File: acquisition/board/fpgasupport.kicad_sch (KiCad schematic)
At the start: 62 parts, among them J1 XILINX_JTAG, U2 XC7A50T-1FTG256C, U6 ICE40UP5K_QFN48

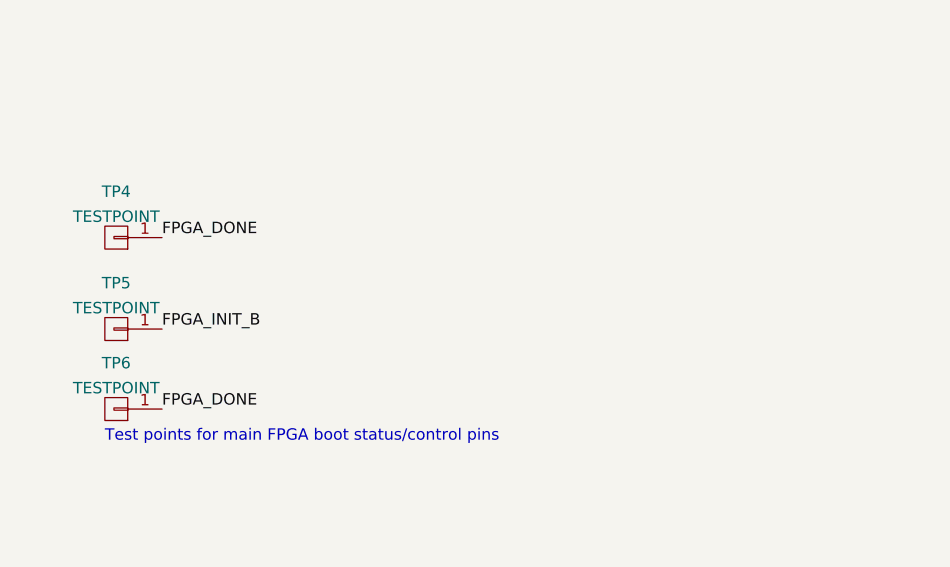
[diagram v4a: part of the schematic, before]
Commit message: Completed schematic after design review, ready for layout
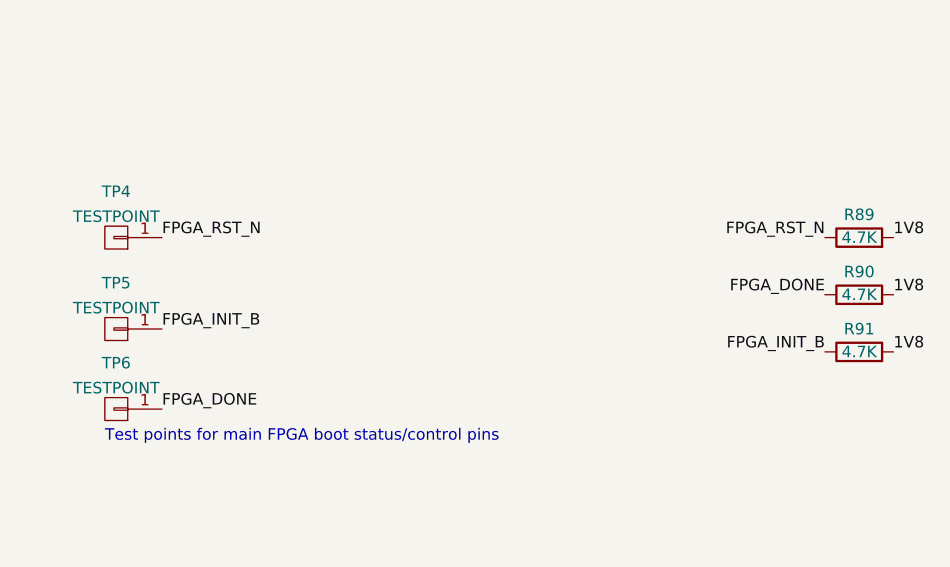
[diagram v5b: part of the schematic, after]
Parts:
- added R89, R90, R91: 4.7K, symbol device:R
- C41, C50: footprint (none) -> azonenberg_pcb:EIA_1210_CAP_NOSILK
- C42, C46: footprint (none) -> azonenberg_pcb:EIA_1206_CAP_NOSILK
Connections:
- net 1V8: now also R89.2, R90.2, R91.2
- net FPGA_DONE: now also R90.1; no longer TP4.1 (P1)
- net FPGA_INIT_B: now also R91.1
- net FPGA_RST_N: now also TP4.1 (P1), R89.1
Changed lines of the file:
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@@
   (title_block
     (title "Digitizer board")
-    (date "2022-07-08")
+    (date "2022-07-17")
     (rev "0.1")
     (company "A. Zonenberg")
@@
     (effects (font (size 1.27 1.27)) (justify right bottom))
   )
-  (label "FPGA_DONE" (at 213.36 129.54 0)
+  (label "FPGA_RST_N" (at 213.36 129.54 0)
     (effects (font (size 1.27 1.27)) (justify left bottom))
   )
@@
     (effects (font (size 1.27 1.27)) (justify right bottom))
   )
+  (label "FPGA_INIT_B" (at 287.02 142.24 180)
+    (effects (font (size 1.27 1.27)) (justify right bottom))
+  )
   (label "GND" (at 55.88 274.32 180)
     (effects (font (size 1.27 1.27)) (justify right bottom))
@@
     (effects (font (size 1.27 1.27)) (justify right bottom))
   )
+  (label "FPGA_DONE" (at 287.02 135.89 180)
+    (effects (font (size 1.27 1.27)) (justify right bottom))
+  )
   (label "1V2" (at 25.4 231.14 180)
+    (effects (font (size 1.27 1.27)) (justify right bottom))
+  )
+  (label "FPGA_RST_N" (at 287.02 129.54 180)
     (effects (font (size 1.27 1.27)) (justify right bottom))
   )
@@
     (effects (font (size 1.27 1.27)) (justify right bottom))
   )
+  (label "1V8" (at 294.64 135.89 0)
+    (effects (font (size 1.27 1.27)) (justify left bottom))
+  )
+  (label "1V8" (at 294.64 142.24 0)
+    (effects (font (size 1.27 1.27)) (justify left bottom))
+  )
   (label "JTAG_TDI" (at 52.07 118.11 180)
     (effects (font (size 1.27 1.27)) (justify right bottom))
@@
   (label "GND" (at 52.07 146.05 180)
     (effects (font (size 1.27 1.27)) (justify right bottom))
+  )
+  (label "1V8" (at 294.64 129.54 0)
+    (effects (font (size 1.27 1.27)) (justify left bottom))
   )
   (label "1V8" (at 57.15 194.31 180)
@@
     )
     (property "Datasheet" "" (id 3) (at 124.46 198.12 0)
+      (effects (font (size 1.27 1.27)) hide)
+    )
+    (pin "1")
+    (pin "2")
+  )
+  (symbol (lib_id "device:R") (at 290.83 129.54 90) (unit 1)
+    (in_bom yes) (on_board yes)
+    (property "Reference" "R89" (id 0) (at 290.83 127 90))
+    (property "Value" "4.7K" (id 1) (at 290.83 129.54 90))
+    (property "Footprint" "" (id 2) (at 290.83 131.318 90)
+      (effects (font (size 1.27 1.27)) hide)
+    )
+    (property "Datasheet" "" (id 3) (at 290.83 129.54 0)
+      (effects (font (size 1.27 1.27)) hide)
+    )
+    (pin "1")
+    (pin "2")
+  )
+  (symbol (lib_id "device:R") (at 290.83 135.89 90) (unit 1)
+    (in_bom yes) (on_board yes)
+    (property "Reference" "R90" (id 0) (at 290.83 133.35 90))
+    (property "Value" "4.7K" (id 1) (at 290.83 135.89 90))
+    (property "Footprint" "" (id 2) (at 290.83 137.668 90)
+      (effects (font (size 1.27 1.27)) hide)
+    )
+    (property "Datasheet" "" (id 3) (at 290.83 135.89 0)
       (effects (font (size 1.27 1.27)) hide)
     )
@@
       (effects (font (size 1.27 1.27)) (justify left))
     )
-    (property "Footprint" "" (id 2) (at 58.1152 186.69 0)
+    (property "Footprint" "azonenberg_pcb:EIA_1206_CAP_NOSILK" (id 2) (at 58.1152 186.69 0)
       (effects (font (size 1.27 1.27)) hide)
     )
@@
     (pin "2")
   )
+  (symbol (lib_id "device:R") (at 290.83 142.24 90) (unit 1)
+    (in_bom yes) (on_board yes)
+    (property "Reference" "R91" (id 0) (at 290.83 139.7 90))
+    (property "Value" "4.7K" (id 1) (at 290.83 142.24 90))
+    (property "Footprint" "" (id 2) (at 290.83 144.018 90)
+      (effects (font (size 1.27 1.27)) hide)
+    )
+    (property "Datasheet" "" (id 3) (at 290.83 142.24 0)
+      (effects (font (size 1.27 1.27)) hide)
+    )
+    (pin "1")
+    (pin "2")
+  )
   (symbol (lib_id "device:C") (at 36.83 246.38 0) (unit 1)
     (in_bom yes) (on_board yes) (fields_autoplaced)
@@
       (effects (font (size 1.27 1.27)) (justify left))
     )
-    (property "Footprint" "" (id 2) (at 84.7852 186.69 0)
+    (property "Footprint" "azonenberg_pcb:EIA_1210_CAP_NOSILK" (id 2) (at 84.7852 186.69 0)
       (effects (font (size 1.27 1.27)) hide)
     )
@@
       (effects (font (size 1.27 1.27)) (justify left))
     )
-    (property "Footprint" "" (id 2) (at 58.1152 172.72 0)
+    (property "Footprint" "azonenberg_pcb:EIA_1210_CAP_NOSILK" (id 2) (at 58.1152 172.72 0)
       (effects (font (size 1.27 1.27)) hide)
     )
@@
       (effects (font (size 1.27 1.27)) (justify left))
     )
-    (property "Footprint" "" (id 2) (at 72.0852 186.69 0)
-      (effects (font (size 1.27 1.27)) hide)
-    )
+    (property "Footprint" "azonenberg_pcb:EIA_1206_CAP_NOSILK" (id 2) (at 72.0852 186.69 0)
+      (effects (font (size 1.27 1.27)) hide)
+    )

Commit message: Finished footprint assignment
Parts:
- L2: footprint (none) -> azonenberg_pcb:EIA_0603_INDUCTOR_NOSILK
- R89, R90, R91: footprint (none) -> azonenberg_pcb:EIA_0402_RES_NOSILK
- U6: footprint (none) -> azonenberg_pcb:QFN_48_0.5MM_7x7MM
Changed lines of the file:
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@@
   (title_block
     (title "Digitizer board")
-    (date "2022-07-17")
+    (date "2023-01-29")
     (rev "0.1")
     (company "A. Zonenberg")
@@
     (property "Reference" "R89" (id 0) (at 290.83 127 90))
     (property "Value" "4.7K" (id 1) (at 290.83 129.54 90))
-    (property "Footprint" "" (id 2) (at 290.83 131.318 90)
+    (property "Footprint" "azonenberg_pcb:EIA_0402_RES_NOSILK" (id 2) (at 290.83 131.318 90)
       (effects (font (size 1.27 1.27)) hide)
     )
@@
     (property "Reference" "R90" (id 0) (at 290.83 133.35 90))
     (property "Value" "4.7K" (id 1) (at 290.83 135.89 90))
-    (property "Footprint" "" (id 2) (at 290.83 137.668 90)
+    (property "Footprint" "azonenberg_pcb:EIA_0402_RES_NOSILK" (id 2) (at 290.83 137.668 90)
       (effects (font (size 1.27 1.27)) hide)
     )
@@
       (effects (font (size 1.016 1.016)))
     )
-    (property "Footprint" "" (id 2) (at 33.02 231.14 0)
+    (property "Footprint" "azonenberg_pcb:EIA_0603_INDUCTOR_NOSILK" (id 2) (at 33.02 231.14 0)
       (effects (font (size 1.524 1.524)) hide)
     )
@@
     (property "Reference" "R91" (id 0) (at 290.83 139.7 90))
     (property "Value" "4.7K" (id 1) (at 290.83 142.24 90))
-    (property "Footprint" "" (id 2) (at 290.83 144.018 90)
+    (property "Footprint" "azonenberg_pcb:EIA_0402_RES_NOSILK" (id 2) (at 290.83 144.018 90)
       (effects (font (size 1.27 1.27)) hide)
     )
@@
       (effects (font (size 1.27 1.27)) (justify left))
     )
-    (property "Footprint" "" (id 2) (at 57.15 234.95 0)
-      (effects (font (size 1.27 1.27)) hide)
-    )
+    (property "Footprint" "azonenberg_pcb:QFN_48_0.5MM_7x7MM" (id 2) (at 57.15 234.95 0)
+      (effects (font (size 1.27 1.27)) hide)
+    )
